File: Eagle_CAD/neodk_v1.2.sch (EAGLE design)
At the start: 73 parts, among them J1 SWD, J2 Power 5V..12V DC, J3 FC68131, J4 S2B-XH-A(LF)(SN), J5 S2B-XH-A(LF)(SN), Q1 IRLML6344TRPBF, Q2 IRLML6344TRPBF, Q3 PMV50EPEAR, SW2 FSMRA6JH, U1 SGM61410XN6G/TR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

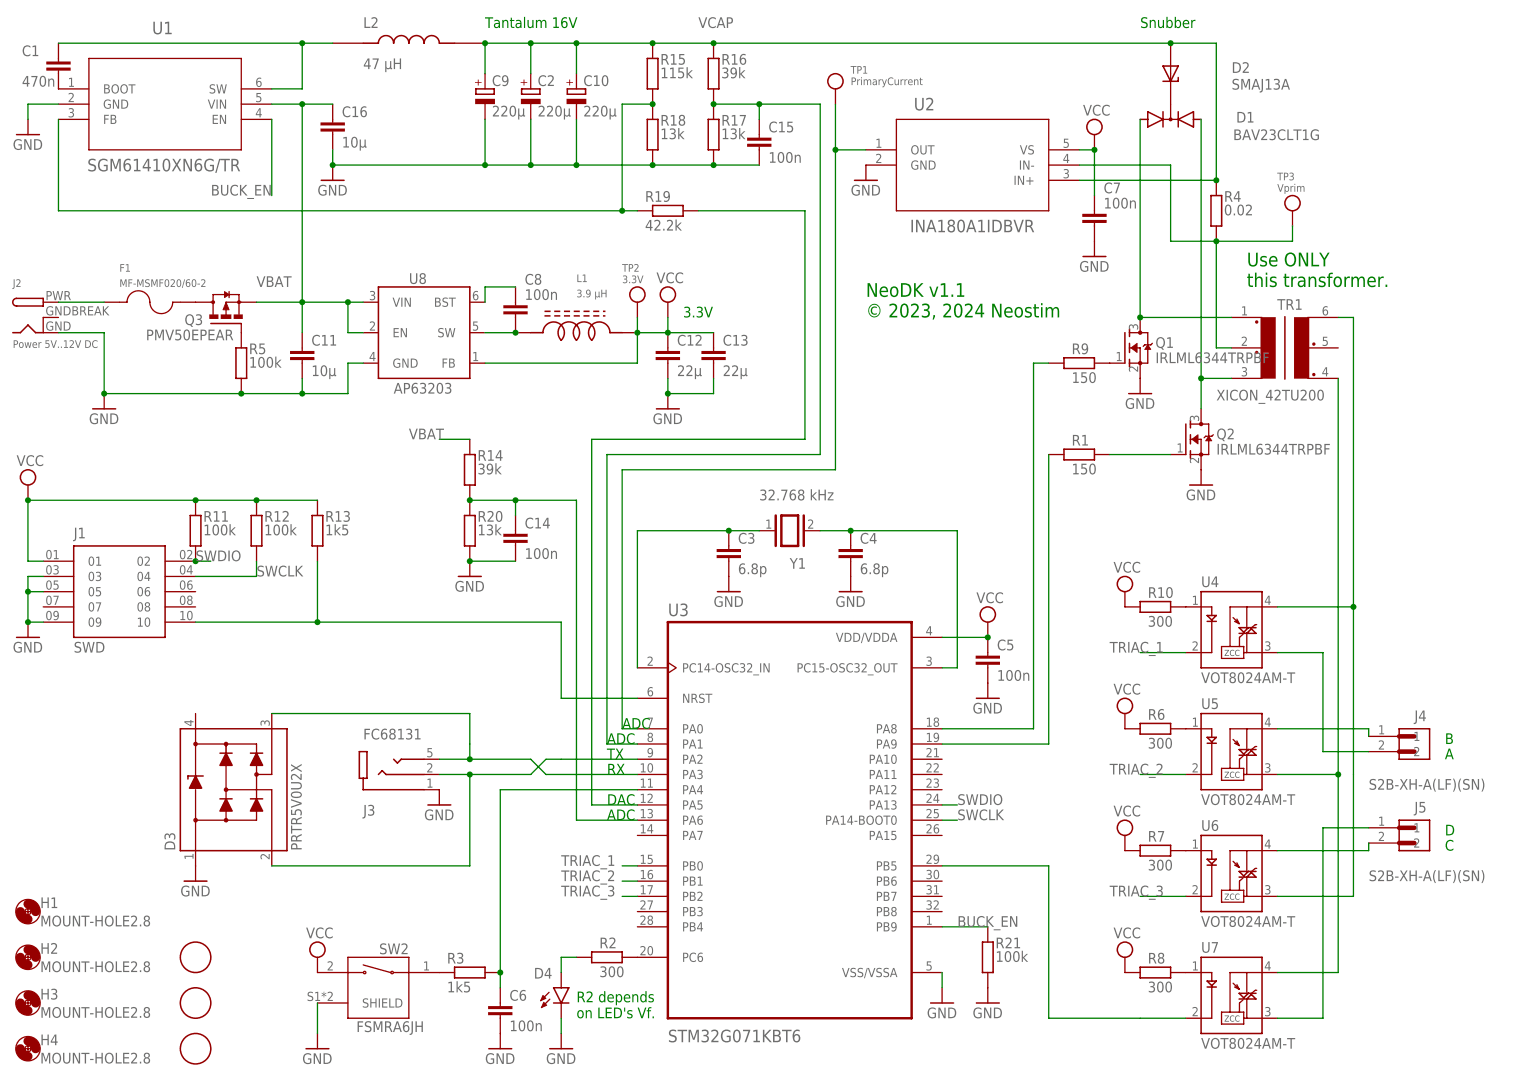
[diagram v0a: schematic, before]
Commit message: Added feature to switch to bootloader.
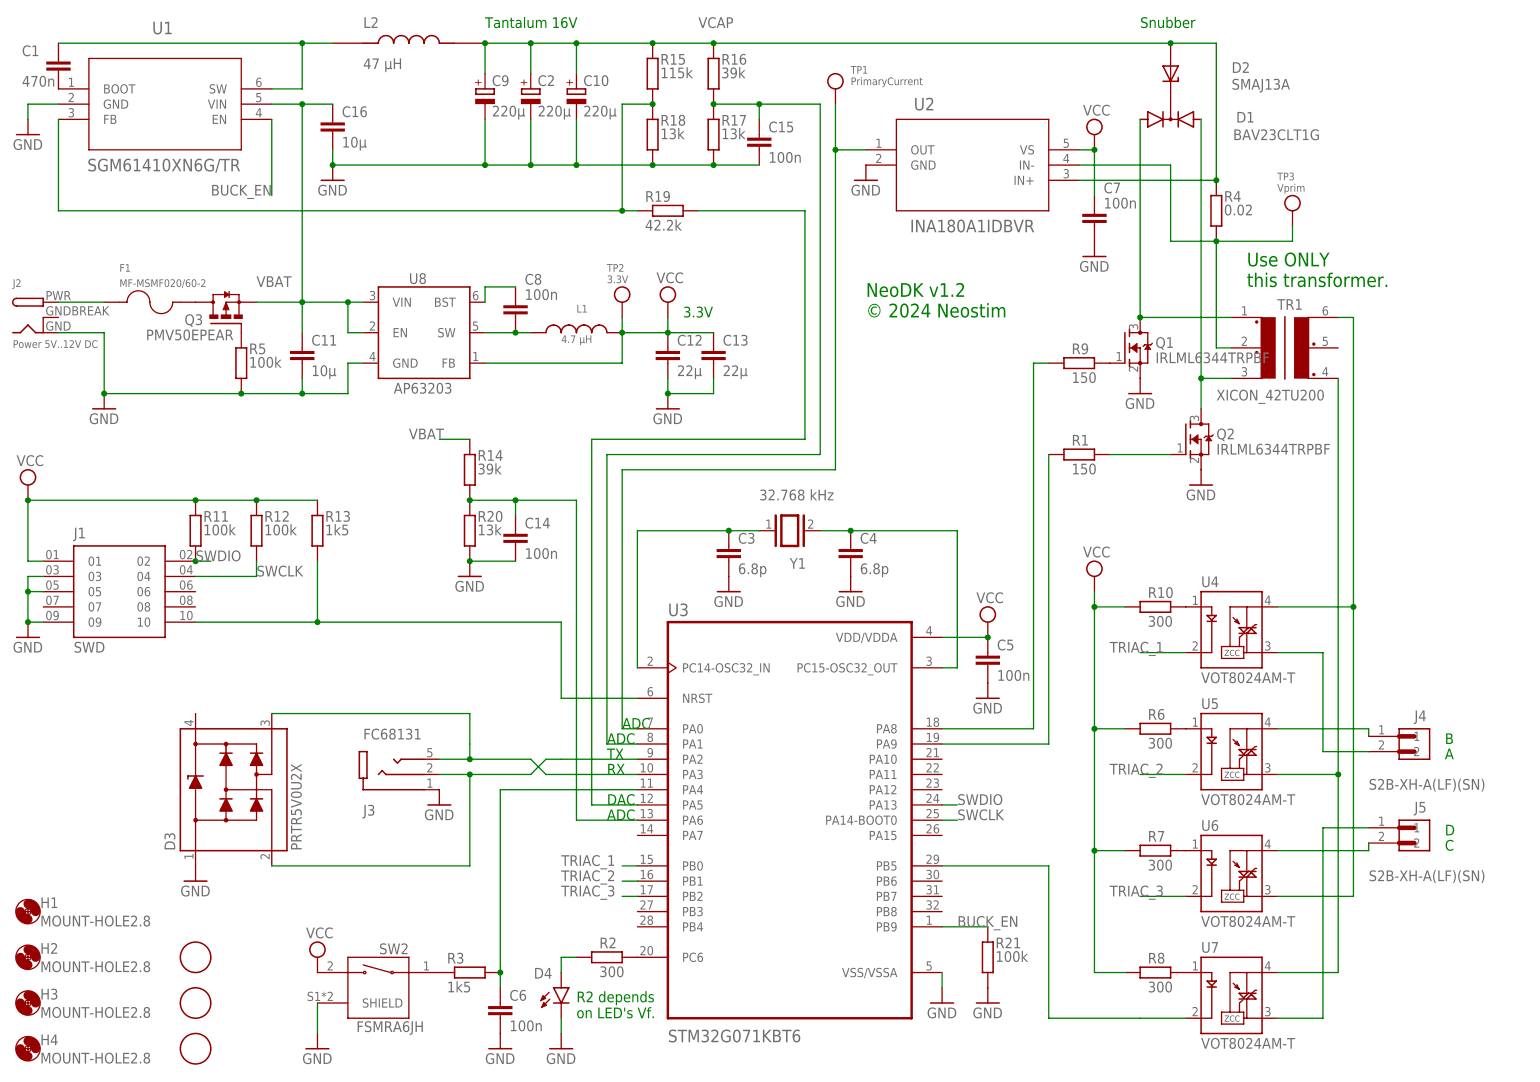
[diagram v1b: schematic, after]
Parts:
- L1: value 3.9 µH -> 4.7 µH; device SRR4818A-3R9Y:SRR4818A-3R9Y -> VLS5045EX-4R7M:VLS5045EX-4R7M
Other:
- note added: "NeoDK v1.2 © 2024 Neostim"
- note removed: "NeoDK v1.1 © 2023, 2024 Neostim"
- moved on the sheet: L1, TP2
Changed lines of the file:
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@@
 <part name="GND15" library="supply1" library_urn="urn:adsk.eagle:library:371" deviceset="GND" device=""/>
 <part name="SUPPLY6" library="supply2" library_urn="urn:adsk.eagle:library:372" deviceset="VCC" device=""/>
-<part name="SUPPLY8" library="supply2" library_urn="urn:adsk.eagle:library:372" deviceset="VCC" device=""/>
-<part name="SUPPLY9" library="supply2" library_urn="urn:adsk.eagle:library:372" deviceset="VCC" device=""/>
 <part name="TP1" library="microbuilder" deviceset="TESTPOINT" device="ROUND1MM" value="PrimaryCurrent"/>
-<part name="SUPPLY13" library="supply2" library_urn="urn:adsk.eagle:library:372" deviceset="VCC" device=""/>
 <part name="U3" library="STM32G071KBT6" deviceset="STM32G071KBT6" device="" value="STM32G071KBT6">
 <attribute name="OC_FARNELL" value="3009964"/>
@@
 <attribute name="OC_FARNELL" value="3953982"/>
 </part>
-<part name="L1" library="SRR4818A-3R9Y" deviceset="SRR4818A-3R9Y" device="" value="3.9 µH"/>
+<part name="L1" library="VLS5045EX-4R7M" deviceset="VLS5045EX-4R7M" device="" value="4.7 µH"/>
 <part name="C4" library="rcl" library_urn="urn:adsk.eagle:library:334" deviceset="C-EU" device="C0603" package3d_urn="urn:adsk.eagle:package:23616/2" value="6.8p">
 <spice>
@@
 <text x="195.58" y="53.34" size="2.286" layer="91" ratio="12">Use ONLY
 this transformer.</text>
-<text x="132.08" y="48.26" size="2.286" layer="91" ratio="10">NeoDK v1.1
-© 2023, 2024 Neostim</text>
+<text x="132.08" y="48.26" size="2.286" layer="91" ratio="10">NeoDK v1.2
+© 2024 Neostim</text>
 <text x="91.44" y="-20.32" size="1.778" layer="91">ADC</text>
 <text x="88.9" y="-22.86" size="1.778" layer="91">ADC</text>
@@
 <attribute name="VALUE" x="78.74" y="-76.2" size="1.778" layer="96"/>
 </instance>
-<instance part="SUPPLY6" gate="G$1" x="175.26" y="2.54" smashed="yes">
-<attribute name="VALUE" x="173.355" y="5.715" size="1.778" layer="96"/>
-</instance>
-<instance part="SUPPLY8" gate="G$1" x="175.26" y="-38.1" smashed="yes">
-<attribute name="VALUE" x="173.355" y="-34.925" size="1.778" layer="96"/>
-</instance>
-<instance part="SUPPLY9" gate="G$1" x="175.26" y="-58.42" smashed="yes">
-<attribute name="VALUE" x="173.355" y="-55.245" size="1.778" layer="96"/>
+<instance part="SUPPLY6" gate="G$1" x="170.18" y="5.08" smashed="yes">
+<attribute name="VALUE" x="168.275" y="8.255" size="1.778" layer="96"/>
 </instance>
 <instance part="TP1" gate="G$1" x="127" y="83.82" smashed="yes">
 <attribute name="NAME" x="129.54" y="88.9" size="1.27" layer="95"/>
 <attribute name="VALUE" x="129.54" y="86.995" size="1.27" layer="95"/>
-</instance>
-<instance part="SUPPLY13" gate="G$1" x="175.26" y="-17.78" smashed="yes">
-<attribute name="VALUE" x="173.355" y="-14.605" size="1.778" layer="96"/>
 </instance>
 <instance part="U3" gate="G$1" x="119.38" y="-35.56" smashed="yes">
@@
 </instance>
 <instance part="L1" gate="G$1" x="83.82" y="45.72" smashed="yes">
-<attribute name="VALUE" x="83.82" y="51.6128" size="1.27" layer="96" ratio="10" rot="SR0"/>
-<attribute name="NAME" x="83.82" y="54.1528" size="1.27" layer="95" ratio="11" rot="SR0"/>
+<attribute name="VALUE" x="81.28" y="43.9928" size="1.27" layer="96" ratio="10" rot="SR0"/>
+<attribute name="NAME" x="83.82" y="49.0728" size="1.27" layer="95" ratio="11" rot="SR0"/>
 </instance>
 <instance part="C4" gate="G$1" x="129.54" y="10.16" smashed="yes">
@@
 <attribute name="OC_FARNELL" x="129.54" y="10.16" size="1.778" layer="96" display="off"/>
 </instance>
-<instance part="TP2" gate="G$1" x="93.98" y="48.26" smashed="yes">
-<attribute name="NAME" x="91.44" y="55.88" size="1.27" layer="95"/>
-<attribute name="VALUE" x="91.44" y="53.975" size="1.27" layer="95"/>
+<instance part="TP2" gate="G$1" x="91.44" y="48.26" smashed="yes">
+<attribute name="NAME" x="88.9" y="55.88" size="1.27" layer="95"/>
+<attribute name="VALUE" x="88.9" y="53.975" size="1.27" layer="95"/>
 </instance>
 <instance part="C16" gate="G$1" x="43.18" y="81.28" smashed="yes">
@@
 <segment>
 <pinref part="SUPPLY6" gate="G$1" pin="VCC"/>
+<pinref part="R8" gate="G$1" pin="2"/>
+<wire x1="170.18" y1="-60.96" x2="175.26" y2="-60.96" width="0.1524" layer="91"/>
+<wire x1="170.18" y1="-60.96" x2="170.18" y2="-40.64" width="0.1524" layer="91"/>
 <pinref part="R10" gate="G$1" pin="2"/>
-</segment>
-<segment>
-<pinref part="SUPPLY13" gate="G$1" pin="VCC"/>
+<wire x1="170.18" y1="-40.64" x2="170.18" y2="-20.32" width="0.1524" layer="91"/>
+<wire x1="170.18" y1="-20.32" x2="170.18" y2="0" width="0.1524" layer="91"/>
+<wire x1="170.18" y1="0" x2="170.18" y2="2.54" width="0.1524" layer="91"/>
+<wire x1="175.26" y1="0" x2="170.18" y2="0" width="0.1524" layer="91"/>
+<junction x="170.18" y="0"/>
+<pinref part="R7" gate="G$1" pin="2"/>
+<wire x1="175.26" y1="-40.64" x2="170.18" y2="-40.64" width="0.1524" layer="91"/>
+<junction x="170.18" y="-40.64"/>
 <pinref part="R6" gate="G$1" pin="2"/>
-</segment>
-<segment>
-<pinref part="SUPPLY8" gate="G$1" pin="VCC"/>
-<pinref part="R7" gate="G$1" pin="2"/>
-</segment>
-<segment>
-<pinref part="SUPPLY9" gate="G$1" pin="VCC"/>
-<pinref part="R8" gate="G$1" pin="2"/>
+<wire x1="175.26" y1="-20.32" x2="170.18" y2="-20.32" width="0.1524" layer="91"/>
+<junction x="170.18" y="-20.32"/>
 </segment>
 <segment>
@@
 <wire x1="99.06" y1="48.26" x2="99.06" y2="45.72" width="0.1524" layer="91"/>
 <pinref part="U8" gate="G$1" pin="FB"/>
-<wire x1="68.58" y1="40.64" x2="93.98" y2="40.64" width="0.1524" layer="91"/>
+<wire x1="68.58" y1="40.64" x2="91.44" y2="40.64" width="0.1524" layer="91"/>
 <pinref part="TP2" gate="G$1" pin="P$1"/>
-<wire x1="93.98" y1="40.64" x2="93.98" y2="45.72" width="0.1524" layer="91"/>
+<wire x1="91.44" y1="40.64" x2="91.44" y2="45.72" width="0.1524" layer="91"/>
 <pinref part="L1" gate="G$1" pin="2"/>
-<wire x1="93.98" y1="45.72" x2="93.98" y2="48.26" width="0.1524" layer="91"/>
-<junction x="93.98" y="45.72"/>
-<wire x1="93.98" y1="45.72" x2="99.06" y2="45.72" width="0.1524" layer="91"/>
+<wire x1="91.44" y1="45.72" x2="91.44" y2="48.26" width="0.1524" layer="91"/>
+<junction x="91.44" y="45.72"/>
+<wire x1="91.44" y1="45.72" x2="99.06" y2="45.72" width="0.1524" layer="91"/>
 </segment>
 </net>
@@
 </segment>
 </net>
-<net name="N$35" class="0">
-<segment>
-<pinref part="U8" gate="G$1" pin="SW"/>
-<pinref part="C8" gate="G$1" pin="2"/>
-<wire x1="68.58" y1="45.72" x2="73.66" y2="45.72" width="0.1524" layer="91"/>
-<pinref part="L1" gate="G$1" pin="1"/>
-<junction x="73.66" y="45.72"/>
-</segment>
-</net>
 <net name="N$36" class="0">
 <segment>
@@
 </segment>
 </net>
+<net name="N$25" class="0">
+<segment>
+<pinref part="U8" gate="G$1" pin="SW"/>
+<pinref part="L1" gate="G$1" pin="1"/>
+<wire x1="68.58" y1="45.72" x2="73.66" y2="45.72" width="0.1524" layer="91"/>
+<pinref part="C8" gate="G$1" pin="2"/>
+<wire x1="73.66" y1="45.72" x2="76.2" y2="45.72" width="0.1524" layer="91"/>
+<junction x="73.66" y="45.72"/>
+</segment>
+</net>
